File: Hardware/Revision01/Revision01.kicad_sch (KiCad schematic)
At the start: 32 parts, among them J1 Battery connector, SW1 SW_SPST_LED, U1 NCP1117LPST50T3G, U2 NUCLEO-L476RG

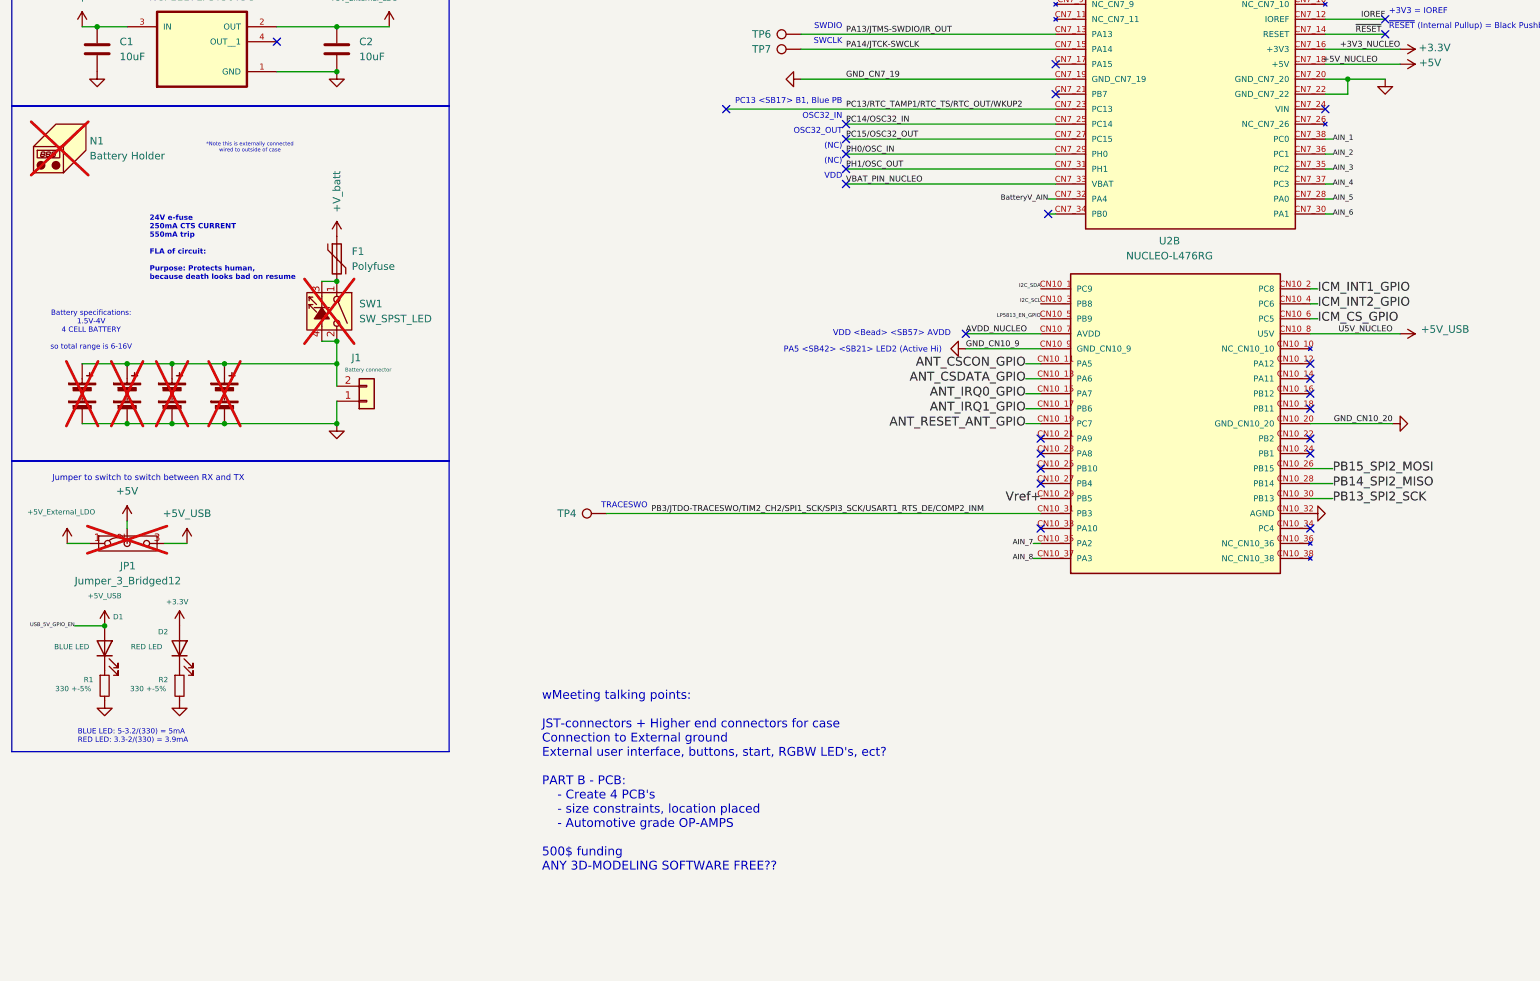
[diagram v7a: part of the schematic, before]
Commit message: Started working on PART B schematic, making small changes on PART A
ADC uncertainty calculated to be 1.22%
Added External GPIO's that may or may not use
	 start/stop, indication RGB leds

Started working on PART B schematic on ALTIUM, properly imported components with footprints
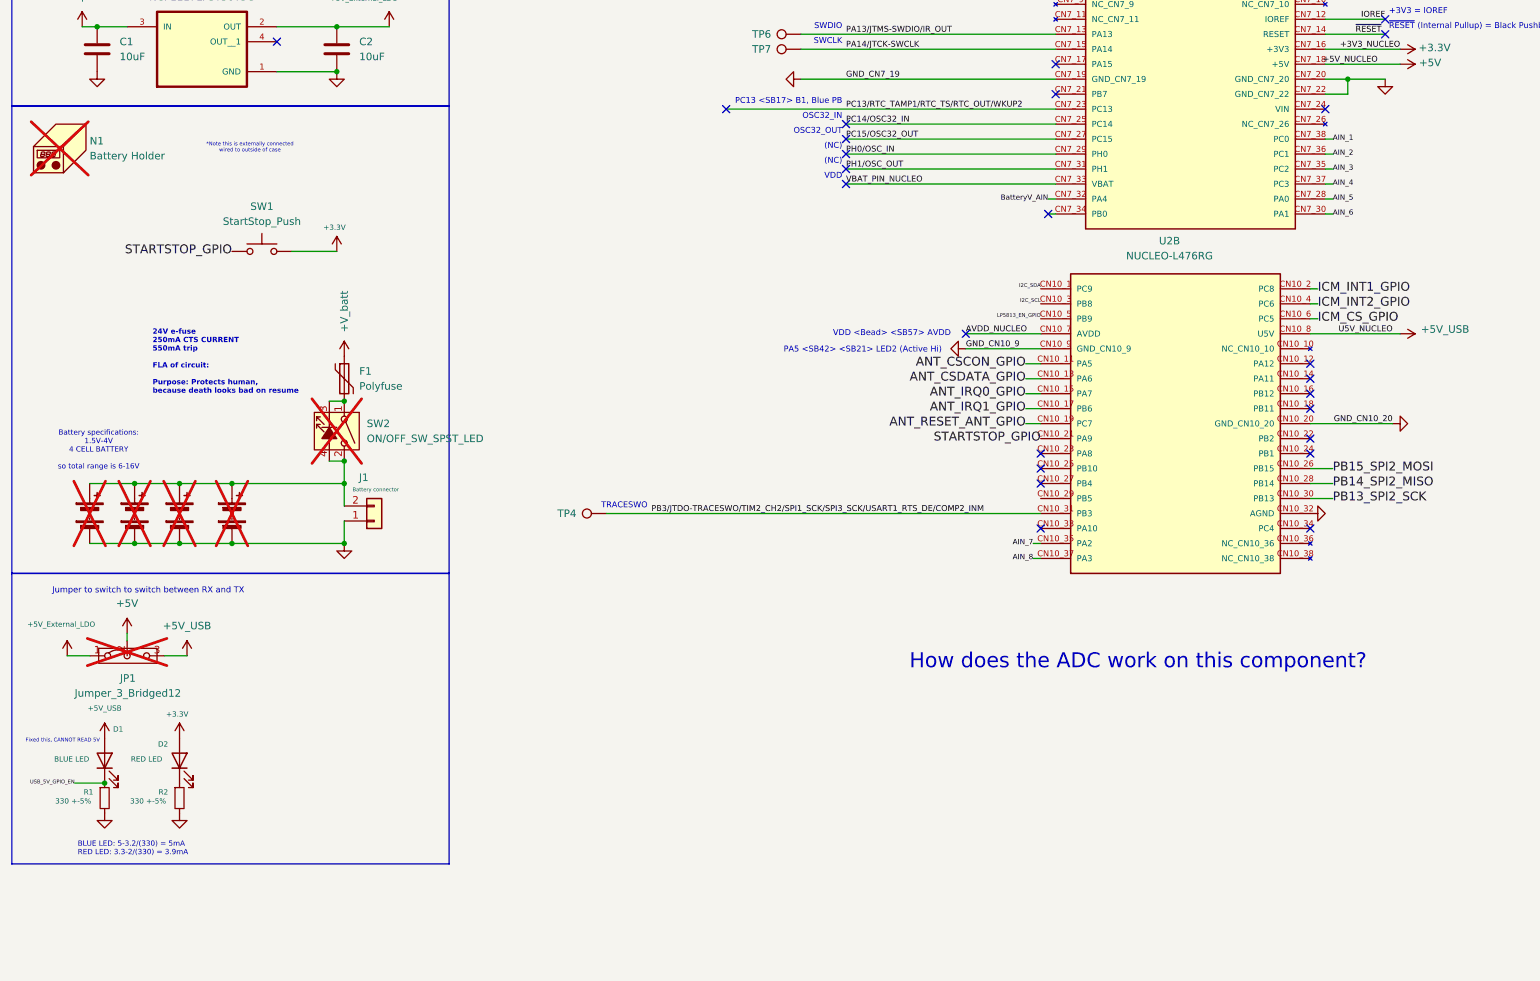
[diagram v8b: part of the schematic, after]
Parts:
- added SW1: StartStop_Push, Connector_PinHeader_2.54mm:PinHeader_1x02_P2.54mm_Vertical, symbol Switch:SW_Push
- SW2: renamed from SW1; value SW_SPST_LED -> ON/OFF_SW_SPST_LED; Distributor link https://www.mouser.ca/ProductDetail/E-Switch/RR11131100-214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 -> https://www.digikey.ca/en/products/detail/e-switch/RB343A11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
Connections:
- net +3.3V: now also SW1.2
- net USB_5V_GPIO_EN: now reaches D1.1 (K), R1.1
- net STARTSTOP_GPIO: now reaches U2.CN10_21 (PA9)
- net STARTSTOP_GPIO: now also SW1.1
- net Vref+: no longer names the net of U2.CN10_29 (PB5)
- no-connect marks 32 -> 31
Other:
- note added: "Fixed this, CANNOT READ 5V"
- note added: "How does the ADC work on this component?"
- note removed: "wMeeting talking points: JST-connectors + Higher end connectors for case Connection to External ground External user interface, buttons, start, RGBW LED's, ect? PART B - PCB: - Create 4 PCB's - size constraints, location placed - Automotive grade OP-AMPS 500$ funding ANY 3D-MODELING SOFTWARE FREE??"
- moved on the sheet: D1, D2, F1, J1, JP1, R1, R2, SW2
